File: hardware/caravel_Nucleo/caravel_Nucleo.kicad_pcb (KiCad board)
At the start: 2 copper layers, 68.1 x 92.5 mm, 90 parts, among them J1 USB_B_Micro - 10118193-0001LF, J10 Conn_01x11_Female, J11 Conn_01x02, J12 Conn_01x02_Male, J2 Conn_01x02_Female, J3 Conn_01x02_Male, J4 Conn_01x04_Female, J5 Conn_01x02_Male, J6 Conn_01x02_Male, J7 Conn_01x06_Female, J8 Conn_01x03, J9 Conn_01x03, SW1 SW_Push - SKQGADE010, T1 Logo, T2 Logo, U1 FT232H, U10 MCP4661, U11 TAR5SxxU_SOT353F, U12 NUCLEO144-F746ZG, U2 SN74LVC1G125DCKR, U3 SN74LVC1G125DCKR, U4 MCP1319MT-29LE-OT, U5 TAR5SxxU_SOT353F, U6 TAR5SxxU_SOT353F, U7 W25Q32FVSS, U8 caravel_breakout, U9 MIC2211-AAYML-TR, X1 DSC6001_10MHZ, Y1 CSTNE12M0GH5L000R0

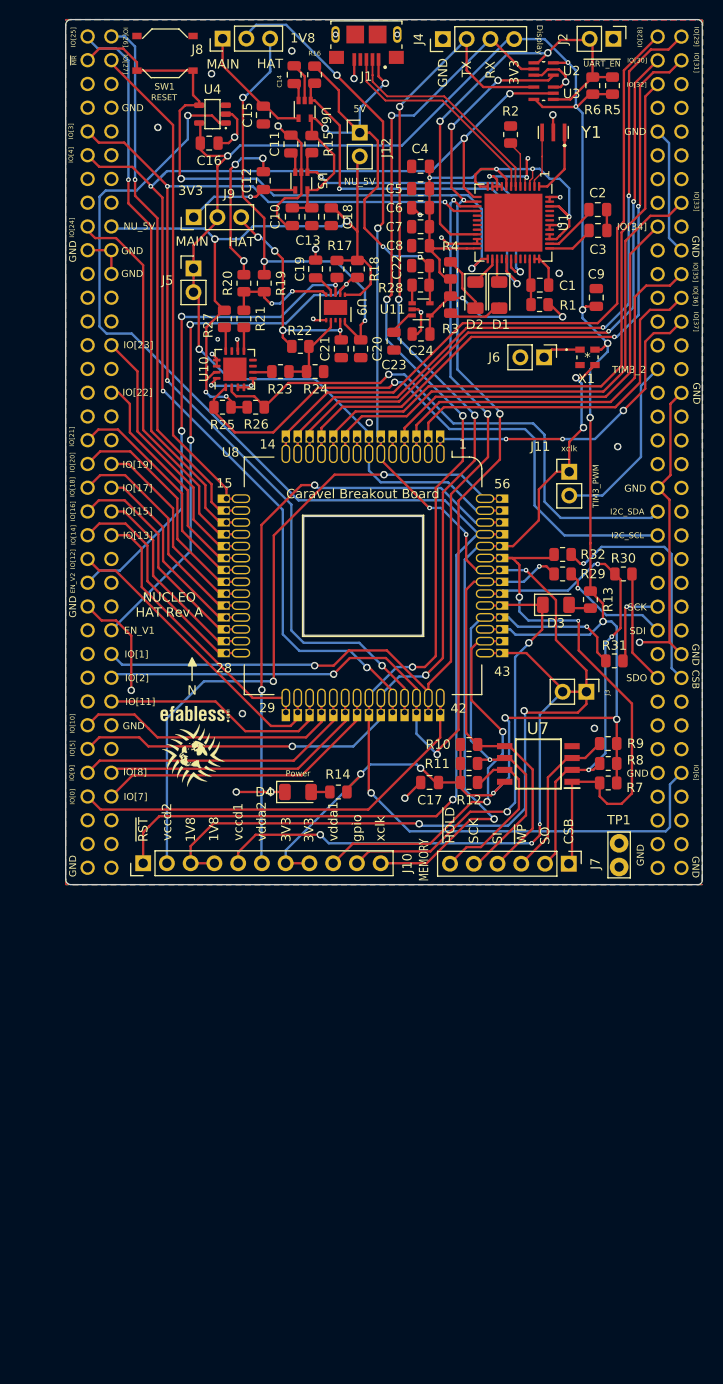
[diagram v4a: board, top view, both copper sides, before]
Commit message: update gpio_config_builder.py and gpio_config_io.c to not generate n_bits value
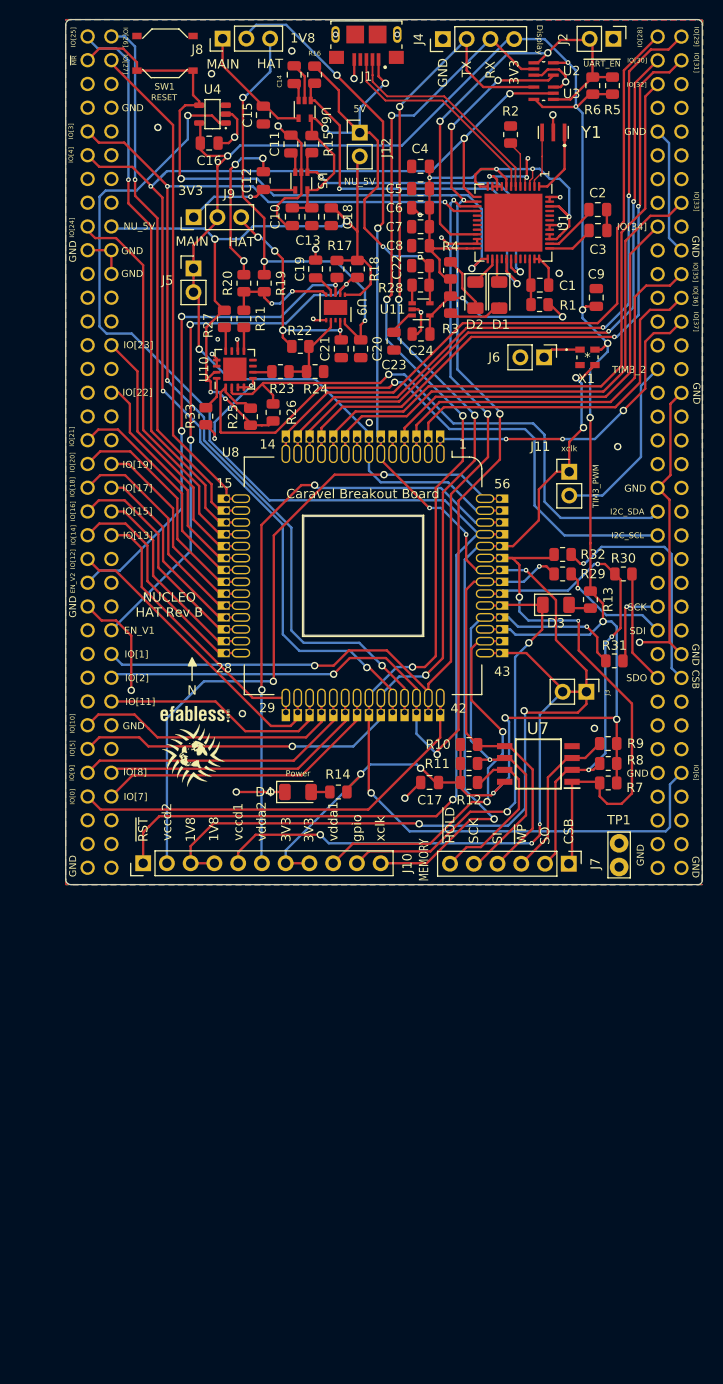
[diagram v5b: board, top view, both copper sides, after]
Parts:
- added R33: 0, Resistor_SMD:R_0805_2012Metric, F.Cu at (115.0, 59.8)
- moved R25 3.16 mm to (119.8, 59.8), turned to 90 degrees
- moved R26 1.94 mm to (122.2, 59.4), turned to 90 degrees
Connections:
- U10 pad 16: GND -> Net-(R33-Pad2)
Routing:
- net I2C4_SCL: track 64.7 -> 68.9 mm
- net GND: track 168.2 -> 172.0 mm
- net Net-(R33-Pad2): track 0.00 -> 3.62 mm
- net NU_5V: track 77.3 -> 80.7 mm
- net ~{RST}: track 152.9 -> 154.8 mm
- net I2C4_SDA: track 59.0 -> 60.5 mm
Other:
- board text added: "NUCLEO HAT Rev B"
- board text removed: "NUCLEO HAT Rev A"
